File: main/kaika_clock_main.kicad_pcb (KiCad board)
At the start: 2 copper layers, 128 x 32 mm, 60 parts, among them J1 Conn_01x05, J2 Conn_01x04, P1 USB-C-SMD_TYPE-C16PIN_C393939, Q1 Q_NPN_BEC, SW1 SW-1101-B-W, SW2 TC-1102N-C-QL-B, SW3 TC-1102N-C-QL-B, U1 AMS1117-3.3, U2 STM32F103C8Tx, U3 DS3231MZ, U4 DHT11_OR_22, Y1 8MHZ

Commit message: modify the main
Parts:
- renumbered JP1 to BOOT0, JP2 to BOOT1
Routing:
- net GND: track 431.2 -> 427.5 mm, vias 52 -> 50
- net VCC: vias 9 -> 8
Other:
- board text added: "2021-01-07"
- board text added: "3.3V"
- board text added: "5V"
- board text added: "Main Design By Team Kaika"
- board text added: "lilili"
- board text removed: "+3.3V"
- board text removed: "+5V"
- board text removed: "2020-12-31"

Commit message: modify the main
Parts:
- removed SW1: SW-1101-B-W, Kaka-footprints:SW-SMD_L6.2-W3.6-LS8.0
- added RESET: Jumper_NO_Small, Jumper:SolderJumper-2_P1.3mm_Open_Pad1.0x1.5mm, F.Cu at (210.1, 129.2)
- BZ1: footprint Buzzer_Beeper:Buzzer_12x9.5RM7.6 -> Kaka-footprints:BUZZER-TH_BD12.0-P6.50-D0.6-FD
- moved BZ1 3.46 mm to (118.9, 106.5)
- renumbered BOOT0 to JP1, BOOT1 to JP2
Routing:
- net +3V3: track 329.4 -> 328.1 mm
- net Net-(BZ1-Pad2): track 5.13 -> 5.88 mm
- net GND: track 427.5 -> 427.4 mm, vias 50 -> 52
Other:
- board text added: "2021-01-08"
- board text added: "Design By Team Kaika V6.0"
- board text added: "V6.0"
- board text removed: "2021-01-07"
- board text removed: "Design By Team Kaika V5.0"
- board text removed: "V5.0"

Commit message: modify the main
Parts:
- removed C15: 100nf, Capacitor_SMD:C_0805_2012Metric_Pad1.18x1.45mm_HandSolder
- BT1: footprint Kaka-footprints:BAT-SMD_CR2032-3V -> Kaka-footprints:BAT-TH_BS-2-1
- moved D2 11.3 mm to (145.6, 123.4)
- moved R5 7.48 mm to (135.5, 102.6), turned to 180 degrees
- moved U3 5.60 mm to (138.2, 107.3)
- moved R6 3.42 mm to (139.8, 102.6), turned to 0 degrees
- moved BT1 2.69 mm to (130.8, 120.6)
- moved C11 2.37 mm to (128.7, 106.0)
- moved BZ1 0.46 mm to (118.5, 106.2)
- moved C4 0.06 mm to (166.1, 114.5)
- renumbered RESET to JP3
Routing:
- net Net-(BT1-Pad1): track 54.2 -> 7.29 mm, vias 4 -> 0
- net GND: track 427.4 -> 444.1 mm
- net +3V3: track 328.1 -> 317.8 mm, vias 25 -> 27
- net Net-(D2-Pad3): track 12.7 -> 21.2 mm
- net I2C1_SCL: track 28.4 -> 21.1 mm
- net VCC: track 209.1 -> 212.5 mm
- net I2C1_SDA: track 31.2 -> 28.4 mm

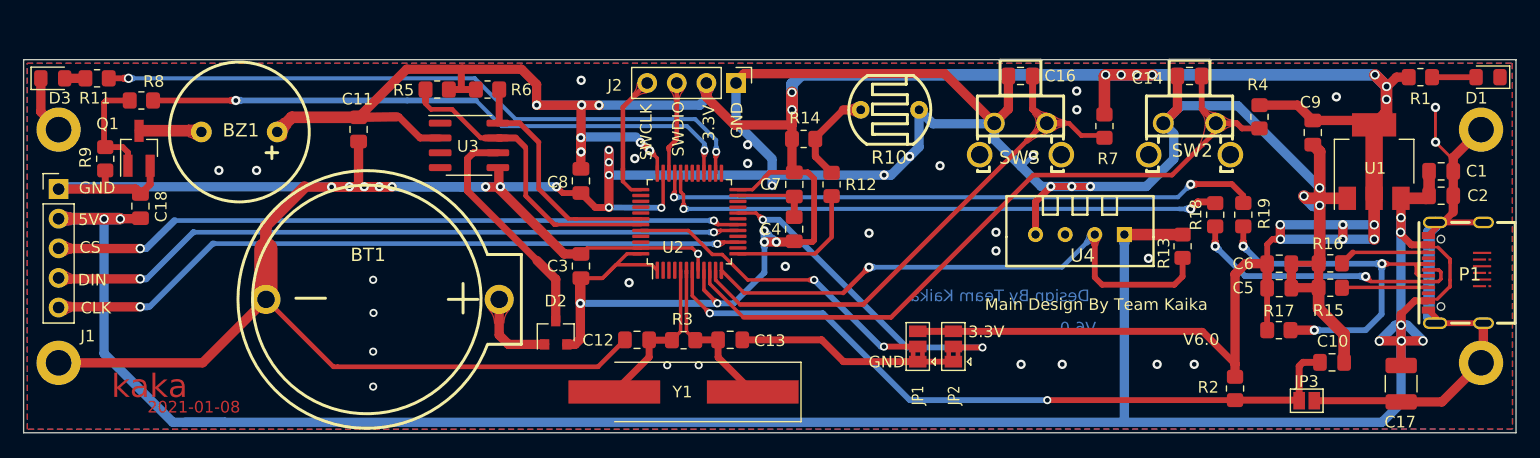
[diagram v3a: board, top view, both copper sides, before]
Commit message: change dht11 vcc to 3.3v
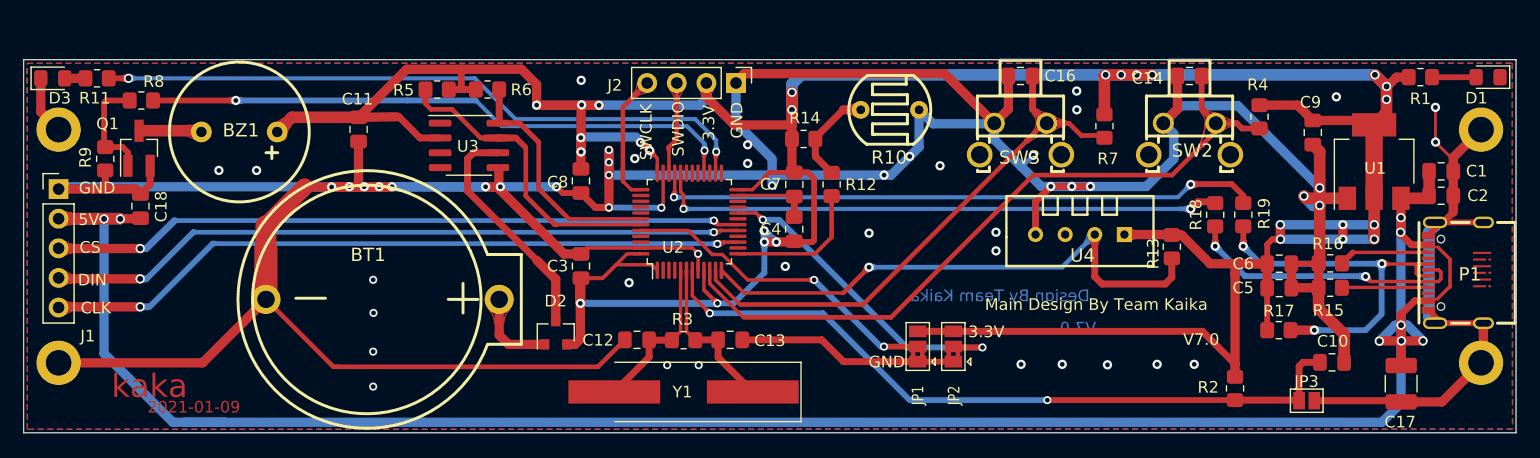
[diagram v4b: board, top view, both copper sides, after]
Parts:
- R13: value 4.7K -> 10K
- moved R13 0.92 mm to (198.5, 116.0)
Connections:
- R13 pad 2: VCC -> +3V3
- U4 pad 1: VCC -> +3V3
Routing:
- net VCC: track 212.5 -> 191.6 mm
- net +3V3: track 317.8 -> 330.8 mm
- net TEMP_SENSOR: track 48.9 -> 47.9 mm
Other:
- board text added: "2021-01-09"
- board text added: "Design By Team Kaika V7.0"
- board text added: "V7.0"
- board text removed: "2021-01-08"
- board text removed: "Design By Team Kaika V6.0"
- board text removed: "V6.0"

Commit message: modify the main borad
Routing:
- net Net-(P1-PadA6): track 33.9 -> 35.3 mm
- net GND: vias 52 -> 53
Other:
- board text added: "Design By Team Kaika V 7.0"
- board text added: "V 7.0"
- board text removed: "Design By Team Kaika V7.0"
- board text removed: "V7.0"

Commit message: modify the main
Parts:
- moved C9 35.6 mm to (181.3, 126.5), turned to 0 degrees
- moved R13 19.6 mm to (180.4, 123.5), turned to 270 degrees
- moved JP1 15.1 mm to (191.8, 125.1)
- moved C10 14.3 mm to (198.6, 121.7), turned to 270 degrees
- moved R2 10.4 mm to (195.8, 121.7)
- moved JP3 9.97 mm to (200.7, 125.8), turned to 270 degrees
- moved C16 9.81 mm to (192.1, 108.7)
- moved C6 9.70 mm to (214.8, 110.9), turned to 180 degrees
- moved C5 9.63 mm to (214.8, 113.1), turned to 180 degrees
- moved R17 9.61 mm to (207.3, 113.6), turned to 180 degrees
- moved U4 9.46 mm to (181.7, 118.2), turned to 0 degrees
- moved JP2 9.07 mm to (188.8, 125.1)
- moved SW3 8.95 mm to (194.1, 104.2)
- moved C14 7.79 mm to (202.9, 108.6)
- moved R7 5.36 mm to (197.2, 108.6), turned to 180 degrees
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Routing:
- net BOOT0: track 28.3 -> 54.4 mm
- net +3V3: track 330.8 -> 306.7 mm, vias 27 -> 14
- net TEMP_SENSOR: track 47.9 -> 29.6 mm
- net GND: track 444.1 -> 461.5 mm, vias 53 -> 50
- net KEY2: track 47.5 -> 58.1 mm, vias 0 -> 1
- net Net-(R10-Pad2): track 8.47 -> 17.9 mm, vias 0 -> 1
- net Net-(P1-PadA6): track 35.3 -> 27.9 mm, vias 3 -> 2
- net BOOT1: track 28.4 -> 35.1 mm
- net KEY1: track 61.7 -> 67.3 mm, vias 0 -> 1
- net USB_D+: track 52.5 -> 47.1 mm
- net RESET: track 63.2 -> 68.2 mm
- net VCC: track 191.6 -> 196.1 mm
- net USB_D-: track 49.7 -> 47.2 mm
- net Net-(D1-Pad2): track 3.77 -> 1.83 mm
- net LIGHT_SENSOR: track 12.2 -> 13.2 mm
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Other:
- board text added: "2021-01-12"
- board text added: "By Kaikai Team V 8.0"
- board text added: "V 8.0"
- board text added: "V8.0"
- board text removed: "2021-01-09"
- board text removed: "Design By Team Kaika"
- board text removed: "V 7.0"

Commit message: modify the main
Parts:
- moved R18 0.50 mm to (199.6, 116.3)
- moved R19 0.42 mm to (199.6, 113.9)
- moved SW3 0.41 mm to (194.1, 103.8)
- moved SW2 0.38 mm to (204.4, 103.8)
- moved R17 0.19 mm to (207.3, 113.8)
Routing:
- net GND: track 461.5 -> 478.7 mm, vias 50 -> 48
- net VCC: track 196.1 -> 197.9 mm
- net KEY1: track 67.3 -> 68.5 mm
- net Net-(P1-PadA6): track 27.9 -> 28.8 mm
- net KEY2: track 58.1 -> 58.9 mm
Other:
- board text added: "By Kaikai Team V 8.1"
- board text added: "D"
- board text added: "G"
- board text added: "V"
- board text added: "V 8.1"
- board text added: "V8.1"
- board text removed: "By Kaikai Team V 8.0"
- board text removed: "V 8.0"
- board text removed: "V8.0"

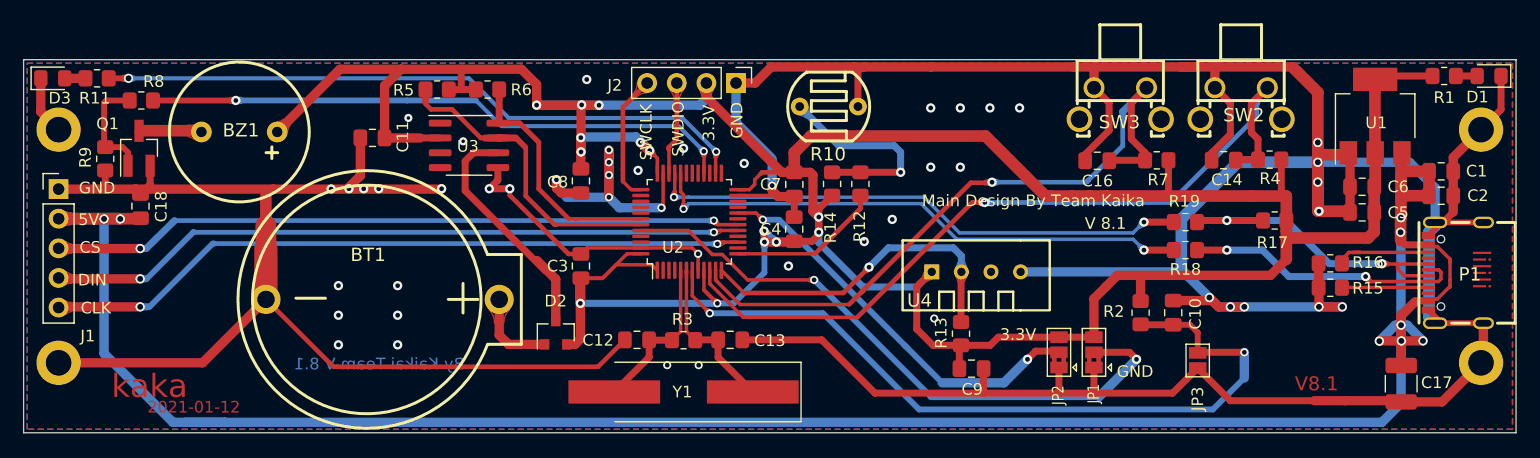
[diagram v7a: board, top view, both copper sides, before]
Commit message: add 18b20 support
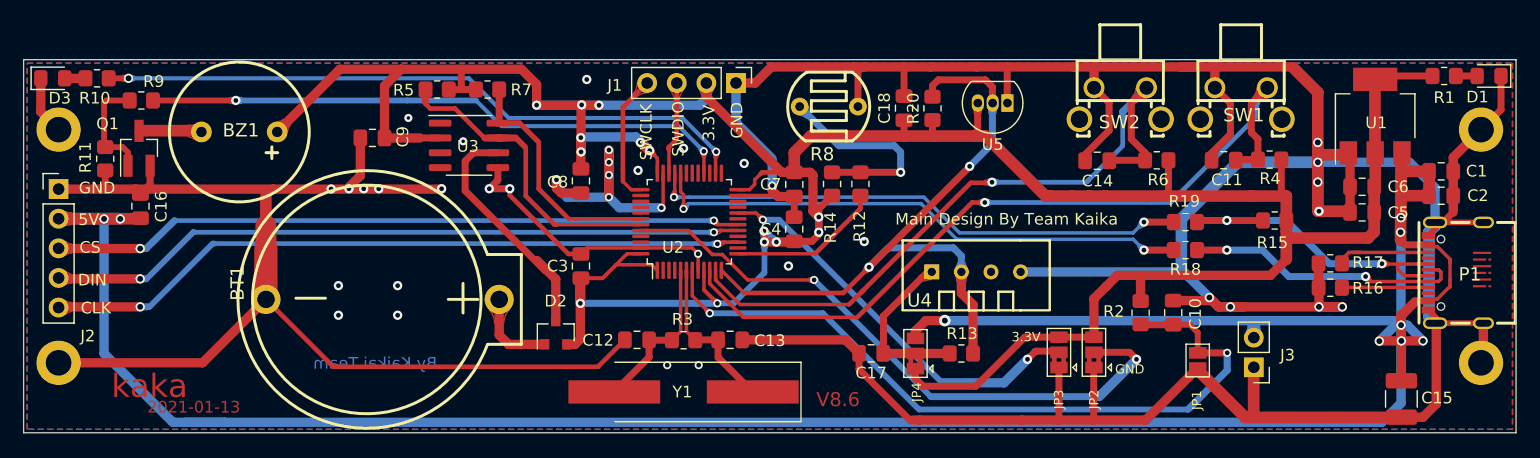
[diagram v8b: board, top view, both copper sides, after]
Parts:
- removed the C9 at (181.3, 126.5)
- added C15: 10uf, Capacitor_SMD:C_1210_3225Metric_Pad1.33x2.70mm_HandSolder, F.Cu at (218.2, 129.1)
- added C18: 100nf, Capacitor_SMD:C_0805_2012Metric_Pad1.18x1.45mm_HandSolder, F.Cu at (175.5, 104.2)
- added J3: Conn_01x02, Connector_PinHeader_2.54mm:PinHeader_1x02_P2.54mm_Vertical, F.Cu at (205.5, 126.4)
- added JP4: Jumper_NC_Dual, Jumper:SolderJumper-3_P1.3mm_Bridged2Bar12_Pad1.0x1.5mm, F.Cu at (176.5, 125.2)
- added R20: 5.1K, Resistor_SMD:R_0805_2012Metric_Pad1.20x1.40mm_HandSolder, F.Cu at (177.9, 104.2)
- added U5: DS18B20, Package_TO_SOT_THT:TO-92_Inline, F.Cu at (184.4, 103.7)
- BT1: footprint Kaka-footprints:BAT-TH_BS-2-1 -> Kaka:BAT-TH_BS-2-1
- C17: value 10uf -> 100nf; footprint Capacitor_SMD:C_1210_3225Metric_Pad1.33x2.70mm_HandSolder -> Capacitor_SMD:C_0805_2012Metric_Pad1.18x1.45mm_HandSolder
- R13: value 10K -> 5.1K
- moved C17 45.5 mm to (172.7, 125.2), turned to 180 degrees
- moved R13 1.70 mm to (180.4, 125.2), turned to 180 degrees
- renumbered C14 to C11, C16 to C14, C18 to C16, C11 to C9, J2 to J1, J1 to J2, JP3 to JP1, JP1 to JP2, JP2 to JP3, R11 to R10, R9 to R11, R17 to R15, R15 to R16, R16 to R17, R7 to R6, R6 to R7, R10 to R8, R8 to R9, SW2 to SW1, SW3 to SW2
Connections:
- C17 pad 1: VCC -> Net-(C17-Pad1)
- P1 pad A8: (no net) -> Net-(P1-PadA8)
- P1 pad B8: (no net) -> Net-(P1-PadB8)
- R13 pad 2: +3V3 -> Net-(C17-Pad1)
- SW1 pad 3: (no net) -> Net-(SW1-Pad3)
- SW1 pad 4: (no net) -> Net-(SW1-Pad4)
- SW2 pad 3: (no net) -> Net-(SW2-Pad3)
- SW2 pad 4: (no net) -> Net-(SW2-Pad4)
- U2 pad 14: (no net) -> Net-(U2-Pad14)
- U2 pad 16: (no net) -> Net-(U2-Pad16)
- U2 pad 19: (no net) -> Net-(U2-Pad19)
- U2 pad 2: (no net) -> Net-(U2-Pad2)
- U2 pad 21: (no net) -> Net-(U2-Pad21)
- U2 pad 22: (no net) -> Net-(U2-Pad22)
- U2 pad 25: (no net) -> Net-(U2-Pad25)
- U2 pad 27: (no net) -> Net-(U2-Pad27)
- U2 pad 29: (no net) -> Net-(U2-Pad29)
- U2 pad 3: (no net) -> Net-(U2-Pad3)
- U2 pad 30: (no net) -> Net-(U2-Pad30)
- U2 pad 31: (no net) -> Net-(U2-Pad31)
- U2 pad 38: (no net) -> Net-(U2-Pad38)
- U2 pad 39: (no net) -> Net-(U2-Pad39)
- U2 pad 4: (no net) -> Net-(U2-Pad4)
- U2 pad 40: (no net) -> Net-(U2-Pad40)
- U2 pad 41: (no net) -> Net-(U2-Pad41)
- U2 pad 45: (no net) -> Net-(U2-Pad45)
- U2 pad 46: (no net) -> Net-(U2-Pad46)
- U3 pad 1: (no net) -> Net-(U3-Pad1)
- U3 pad 3: (no net) -> Net-(U3-Pad3)
- U3 pad 4: (no net) -> Net-(U3-Pad4)
- U4 pad 1: +3V3 -> Net-(C17-Pad1)
- U4 pad 3: (no net) -> Net-(U4-Pad3)
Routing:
- net VCC: track 197.9 -> 244.7 mm, vias 8 -> 9
- net TEMP_SENSOR: track 29.6 -> 59.2 mm, vias 1 -> 2
- net GND: track 478.7 -> 496.2 mm, vias 48 -> 37
- net Net-(C17-Pad1): track 0.00 -> 14.7 mm
- net +3V3: track 306.4 -> 294.7 mm
- net RESET: track 68.2 -> 64.8 mm
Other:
- board text added: "2021-01-13"
- board text added: "By Kaikai Team"
- board text added: "Design By Team Kaika"
- board text added: "V8.6"
- board text removed: "2021-01-12"
- board text removed: "By Kaikai Team V 8.1"
- board text removed: "Design By Team Kaika V 7.0"
- board text removed: "V 8.1"
- board text removed: "V8.1"
